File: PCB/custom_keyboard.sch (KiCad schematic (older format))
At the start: 33 parts

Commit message: Keyboard matrix
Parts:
- removed MX?: MX-NoLED, symbol MX_Alps_Hybrid:MX-NoLED
- added D? (x23): SOD-123, symbol Device:D_Small
- added SW? (x23): CherryMX, symbol CherryMX:CherryMX
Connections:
- net labels added: ROT1_COL, ROT1_ROW, ROT2_COL, ROT2_ROW
- wire segments 104 -> 248

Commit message: RGB LED Matrix
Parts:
- removed D? (x6): SOD-123, symbol Device:D_Small
- removed SW? (x6): CherryMX, symbol CherryMX:CherryMX
- added C? (x92): 0.1uF, symbol Device:C_Small
- added D? (x74): SOD-123, symbol Device:D_Small
- added D? (x92): WS2812B, LED_SMD:LED_WS2812B_PLCC4_5.0x5.0mm_P3.2mm, symbol LED:WS2812B
- added R?: 500, symbol Device:R_Small
- added SW?: ESC, symbol CherryMX:CherryMX
- added SW?: `/~, symbol CherryMX:CherryMX
- added SW?: TAB, symbol CherryMX:CherryMX
- added SW?: CAPS, symbol CherryMX:CherryMX
- added SW?: LSHIFT, symbol CherryMX:CherryMX
- added SW?: 1, symbol CherryMX:CherryMX
- added SW?: Q, symbol CherryMX:CherryMX
- added SW?: A, symbol CherryMX:CherryMX
- added SW?: Z, symbol CherryMX:CherryMX
- added SW?: F1, symbol CherryMX:CherryMX
- added SW?: 2, symbol CherryMX:CherryMX
- added SW?: W, symbol CherryMX:CherryMX
- added SW?: S, symbol CherryMX:CherryMX
- added SW?: X, symbol CherryMX:CherryMX
- added SW?: F2, symbol CherryMX:CherryMX
- added SW?: 3, symbol CherryMX:CherryMX
- added SW?: E, symbol CherryMX:CherryMX
- added SW?: D, symbol CherryMX:CherryMX
- added SW?: C, symbol CherryMX:CherryMX
- added SW?: F3, symbol CherryMX:CherryMX
- added SW?: 4, symbol CherryMX:CherryMX
- added SW?: R, symbol CherryMX:CherryMX
- added SW?: F, symbol CherryMX:CherryMX
- added SW?: V, symbol CherryMX:CherryMX
- added SW?: B, symbol CherryMX:CherryMX
- added SW?: G, symbol CherryMX:CherryMX
- added SW?: T, symbol CherryMX:CherryMX
- added SW?: 5, symbol CherryMX:CherryMX
- added SW?: F4, symbol CherryMX:CherryMX
- added SW?: N, symbol CherryMX:CherryMX
- added SW?: M, symbol CherryMX:CherryMX
- added SW?: ,/<, symbol CherryMX:CherryMX
- added SW?: F5, symbol CherryMX:CherryMX
- added SW?: 6, symbol CherryMX:CherryMX
- added SW?: Y, symbol CherryMX:CherryMX
- added SW?: H, symbol CherryMX:CherryMX
- added SW?: J, symbol CherryMX:CherryMX
- added SW?: U, symbol CherryMX:CherryMX
- added SW?: 7, symbol CherryMX:CherryMX
- added SW?: F6, symbol CherryMX:CherryMX
- added SW?: F7, symbol CherryMX:CherryMX
- added SW?: 8, symbol CherryMX:CherryMX
- added SW?: I, symbol CherryMX:CherryMX
- added SW?: K, symbol CherryMX:CherryMX
- added SW?: F8, symbol CherryMX:CherryMX
- added SW?: 9, symbol CherryMX:CherryMX
- added SW?: O, symbol CherryMX:CherryMX
- added SW?: L, symbol CherryMX:CherryMX
- added SW?: ./>, symbol CherryMX:CherryMX
- added SW?: F9, symbol CherryMX:CherryMX
- added SW?: F10, symbol CherryMX:CherryMX
- added SW?: F11, symbol CherryMX:CherryMX
- added SW?: F12, symbol CherryMX:CherryMX
- added SW?: PSCR, symbol CherryMX:CherryMX
- added SW?: 0, symbol CherryMX:CherryMX
- added SW?: -/_, symbol CherryMX:CherryMX
- added SW?: =/+, symbol CherryMX:CherryMX
- added SW?: BACKSPACE, symbol CherryMX:CherryMX
- added SW?: INS, symbol CherryMX:CherryMX
- added SW?: HOME, symbol CherryMX:CherryMX
- added SW?: PGUP, symbol CherryMX:CherryMX
- added SW?: P, symbol CherryMX:CherryMX
- added SW?: [/{, symbol CherryMX:CherryMX
- added SW?: ]/}, symbol CherryMX:CherryMX
- added SW?: \\, symbol CherryMX:CherryMX
- added SW?: DELETE, symbol CherryMX:CherryMX
- added SW?: END, symbol CherryMX:CherryMX
- added SW?: PGDN, symbol CherryMX:CherryMX
- added SW?: ;/:, symbol CherryMX:CherryMX
- added SW?: '/\", symbol CherryMX:CherryMX
- added SW?: ENTER, symbol CherryMX:CherryMX
- added SW?: RSHIFT, symbol CherryMX:CherryMX
- added SW?: /, symbol CherryMX:CherryMX
- added SW?: UP, symbol CherryMX:CherryMX
- SW?: value CherryMX -> M1
- SW?: value CherryMX -> M5
- SW?: value CherryMX -> M2
- SW?: value CherryMX -> M3
- SW?: value CherryMX -> M4
- SW?: value CherryMX -> RIGHT
- SW?: value CherryMX -> LCTRL
- SW?: value CherryMX -> LGUI
- SW?: value CherryMX -> LALT
- SW?: value CherryMX -> SPACE
- SW?: value CherryMX -> RALT
- SW?: value CherryMX -> RGUI
- SW?: value CherryMX -> MENU
- SW?: value CherryMX -> RCTRL
- SW?: value CherryMX -> LEFT
- SW?: value CherryMX -> DOWN
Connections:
- net ROT1_COL is gone; now on net COL17: ROT1.S1
- net ROT2_ROW is gone; now on net ROT1_ROW: D?.1 (K)
- net +5V: now also C?.1, C?.1, C?.1, C?.1, C?.1, C?.1, C?.1, C?.1, C?.1, C?.1, C?.1, C?.1, C?.1, C?.1, C?.1, C?.1, C?.1, C?.1, C?.1, C?.1, C?.1, C?.1, C?.1, C?.1, C?.1, C?.1, C?.1, C?.1, C?.1, C?.1, C?.1, C?.1, C?.1, C?.1, C?.1, C?.1, C?.1, C?.1, C?.1, C?.1, C?.1, C?.1, C?.1, C?.1, C?.1, C?.1, C?.1, C?.1, C?.1, C?.1, C?.1, C?.1, C?.1, C?.1, C?.1, C?.1, C?.1, C?.1, C?.1, C?.1, C?.1, C?.1, C?.1, C?.1, C?.1, C?.1, C?.1, C?.1, C?.1, C?.1, C?.1, C?.1, C?.1, C?.1, C?.1, C?.1, C?.1, C?.1, C?.1, C?.1, C?.1, C?.1, C?.1, C?.1, C?.1, C?.1, C?.1, C?.1, C?.1, C?.1, C?.1, C?.1, D?.1 (VDD), D?.1 (VDD), D?.1 (VDD), D?.1 (VDD), D?.1 (VDD), D?.1 (VDD), D?.1 (VDD), D?.1 (VDD), D?.1 (VDD), D?.1 (VDD), D?.1 (VDD), D?.1 (VDD), D?.1 (VDD), D?.1 (VDD), D?.1 (VDD), D?.1 (VDD), D?.1 (VDD), D?.1 (VDD), D?.1 (VDD), D?.1 (VDD), D?.1 (VDD), D?.1 (VDD), D?.1 (VDD), D?.1 (VDD), D?.1 (VDD), D?.1 (VDD), D?.1 (VDD), D?.1 (VDD), D?.1 (VDD), D?.1 (VDD), D?.1 (VDD), D?.1 (VDD), D?.1 (VDD), D?.1 (VDD), D?.1 (VDD), D?.1 (VDD), D?.1 (VDD), D?.1 (VDD), D?.1 (VDD), D?.1 (VDD), D?.1 (VDD), D?.1 (VDD), D?.1 (VDD), D?.1 (VDD), D?.1 (VDD), D?.1 (VDD), D?.1 (VDD), D?.1 (VDD), D?.1 (VDD), D?.1 (VDD), D?.1 (VDD), D?.1 (VDD), D?.1 (VDD), D?.1 (VDD), D?.1 (VDD), D?.1 (VDD), D?.1 (VDD), D?.1 (VDD), D?.1 (VDD), D?.1 (VDD), D?.1 (VDD), D?.1 (VDD), D?.1 (VDD), D?.1 (VDD), D?.1 (VDD), D?.1 (VDD), D?.1 (VDD), D?.1 (VDD), D?.1 (VDD), D?.1 (VDD), D?.1 (VDD), D?.1 (VDD), D?.1 (VDD), D?.1 (VDD), D?.1 (VDD), D?.1 (VDD), D?.1 (VDD), D?.1 (VDD), D?.1 (VDD), D?.1 (VDD), D?.1 (VDD), D?.1 (VDD), D?.1 (VDD), D?.1 (VDD), D?.1 (VDD), D?.1 (VDD), D?.1 (VDD), D?.1 (VDD), D?.1 (VDD), D?.1 (VDD), D?.1 (VDD), D?.1 (VDD)
- net BKL_DATA_IN: now also R?.1
- net COL1: now also SW?.1, SW?.1, SW?.1, SW?.1, SW?.1
- net COL10: now also SW?.1, SW?.1, SW?.1, SW?.1, SW?.1
- net COL11: now also SW?.1, SW?.1, SW?.1, SW?.1, SW?.1
- net COL12: now also SW?.1, SW?.1, SW?.1, SW?.1
- net COL13: now also SW?.1, SW?.1, SW?.1
- net COL14: now also SW?.1, SW?.1, SW?.1, SW?.1, SW?.1
- net COL15: now also SW?.1, SW?.1, SW?.1
- net COL16: now also SW?.1, SW?.1, SW?.1
- net COL17: now also SW?.1, SW?.1
- net COL2: now also SW?.1, SW?.1, SW?.1, SW?.1
- net COL3: now also SW?.1, SW?.1, SW?.1, SW?.1, SW?.1
- net COL4: now also SW?.1, SW?.1, SW?.1, SW?.1, SW?.1
- net COL5: now also SW?.1, SW?.1, SW?.1, SW?.1, SW?.1
- net COL6: now also SW?.1, SW?.1, SW?.1, SW?.1, SW?.1
- net COL7: now also SW?.1, SW?.1, SW?.1, SW?.1, SW?.1
- net COL8: now also SW?.1, SW?.1, SW?.1, SW?.1, SW?.1
- net COL9: now also SW?.1, SW?.1, SW?.1, SW?.1, SW?.1
- net GND: now also C?.2, C?.2, C?.2, C?.2, C?.2, C?.2, C?.2, C?.2, C?.2, C?.2, C?.2, C?.2, C?.2, C?.2, C?.2, C?.2, C?.2, C?.2, C?.2, C?.2, C?.2, C?.2, C?.2, C?.2, C?.2, C?.2, C?.2, C?.2, C?.2, C?.2, C?.2, C?.2, C?.2, C?.2, C?.2, C?.2, C?.2, C?.2, C?.2, C?.2, C?.2, C?.2, C?.2, C?.2, C?.2, C?.2, C?.2, C?.2, C?.2, C?.2, C?.2, C?.2, C?.2, C?.2, C?.2, C?.2, C?.2, C?.2, C?.2, C?.2, C?.2, C?.2, C?.2, C?.2, C?.2, C?.2, C?.2, C?.2, C?.2, C?.2, C?.2, C?.2, C?.2, C?.2, C?.2, C?.2, C?.2, C?.2, C?.2, C?.2, C?.2, C?.2, C?.2, C?.2, C?.2, C?.2, C?.2, C?.2, C?.2, C?.2, C?.2, C?.2, D?.3 (VSS), D?.3 (VSS), D?.3 (VSS), D?.3 (VSS), D?.3 (VSS), D?.3 (VSS), D?.3 (VSS), D?.3 (VSS), D?.3 (VSS), D?.3 (VSS), D?.3 (VSS), D?.3 (VSS), D?.3 (VSS), D?.3 (VSS), D?.3 (VSS), D?.3 (VSS), D?.3 (VSS), D?.3 (VSS), D?.3 (VSS), D?.3 (VSS), D?.3 (VSS), D?.3 (VSS), D?.3 (VSS), D?.3 (VSS), D?.3 (VSS), D?.3 (VSS), D?.3 (VSS), D?.3 (VSS), D?.3 (VSS), D?.3 (VSS), D?.3 (VSS), D?.3 (VSS), D?.3 (VSS), D?.3 (VSS), D?.3 (VSS), D?.3 (VSS), D?.3 (VSS), D?.3 (VSS), D?.3 (VSS), D?.3 (VSS), D?.3 (VSS), D?.3 (VSS), D?.3 (VSS), D?.3 (VSS), D?.3 (VSS), D?.3 (VSS), D?.3 (VSS), D?.3 (VSS), D?.3 (VSS), D?.3 (VSS), D?.3 (VSS), D?.3 (VSS), D?.3 (VSS), D?.3 (VSS), D?.3 (VSS), D?.3 (VSS), D?.3 (VSS), D?.3 (VSS), D?.3 (VSS), D?.3 (VSS), D?.3 (VSS), D?.3 (VSS), D?.3 (VSS), D?.3 (VSS), D?.3 (VSS), D?.3 (VSS), D?.3 (VSS), D?.3 (VSS), D?.3 (VSS), D?.3 (VSS), D?.3 (VSS), D?.3 (VSS), D?.3 (VSS), D?.3 (VSS), D?.3 (VSS), D?.3 (VSS), D?.3 (VSS), D?.3 (VSS), D?.3 (VSS), D?.3 (VSS), D?.3 (VSS), D?.3 (VSS), D?.3 (VSS), D?.3 (VSS), D?.3 (VSS), D?.3 (VSS), D?.3 (VSS), D?.3 (VSS), D?.3 (VSS), D?.3 (VSS), D?.3 (VSS), D?.3 (VSS)
- net ROT1_ROW: now also D?.1 (K), D?.1 (K), D?.1 (K), D?.1 (K), D?.1 (K), D?.1 (K), D?.1 (K), D?.1 (K), D?.1 (K), D?.1 (K), D?.1 (K), D?.1 (K), D?.1 (K), D?.1 (K)
- net ROW1: now also D?.1 (K), D?.1 (K), D?.1 (K), D?.1 (K), D?.1 (K), D?.1 (K), D?.1 (K), D?.1 (K), D?.1 (K), D?.1 (K), D?.1 (K), D?.1 (K), D?.1 (K), D?.1 (K), D?.1 (K), D?.1 (K), D?.1 (K), D?.1 (K)
- net ROW2: now also D?.1 (K), D?.1 (K), D?.1 (K), D?.1 (K), D?.1 (K), D?.1 (K), D?.1 (K), D?.1 (K), D?.1 (K), D?.1 (K), D?.1 (K), D?.1 (K), D?.1 (K), D?.1 (K), D?.1 (K), D?.1 (K), D?.1 (K)
- net ROW3: now also D?.1 (K), D?.1 (K), D?.1 (K), D?.1 (K), D?.1 (K), D?.1 (K), D?.1 (K), D?.1 (K), D?.1 (K), D?.1 (K), D?.1 (K), D?.1 (K), D?.1 (K)
- net ROW4: now also D?.1 (K), D?.1 (K), D?.1 (K), D?.1 (K), D?.1 (K), D?.1 (K), D?.1 (K), D?.1 (K), D?.1 (K), D?.1 (K), D?.1 (K), D?.1 (K), D?.1 (K)
- new net: D?.2 (A), SW?.2 (x74)
- new net: D?.2 (DOUT), D?.4 (DIN) (x82)
- new net: D?.4 (DIN), R?.2
- new net DOUT1: D?.2 (DOUT), D?.4 (DIN)
- new net DOUT2: D?.2 (DOUT), D?.4 (DIN)
- new net DOUT3: D?.2 (DOUT), D?.4 (DIN)
- new net DOUT4: D?.2 (DOUT), D?.4 (DIN)
- new net DOUT5: D?.2 (DOUT), D?.4 (DIN)
- new net DOUT6: D?.2 (DOUT), D?.4 (DIN)
- new net DOUT7: D?.2 (DOUT), D?.4 (DIN)
- new net DOUT8: D?.2 (DOUT), D?.4 (DIN)
- new net DOUT9: D?.2 (DOUT), D?.4 (DIN)
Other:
- note added: "0"
- note added: "1"
- note added: "10"
- note added: "10\n"
- note added: "11"
- note added: "12"
- note added: "13"
- note added: "14"
- note added: "15"
- note added: "16"
- note added: "17"
- note added: "2"
- note added: "3"
- note added: "4"
- note added: "5"
- note added: "6"
- note added: "7"
- note added: "7\n"
- note added: "8"
- note added: "9"
- moved on the sheet: C?, D?, J?, R?, ROT1, ROT2, SW?, U?, Y?

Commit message: Added outlines
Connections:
- net BKL_DATA_IN: now also U?.51 (PA0)
- net COL0: now also U?.47 (PA4)
- net COL1: now also U?.46 (PA5)
- net COL10: now also U?.36 (PC1)
- net COL11: now also U?.35 (PC0)
- net COL14: now also U?.32 (PD7)
- net COL15: now also U?.31 (PD6)
- net COL16: now also U?.30 (PD5)
- net COL17: now also U?.29 (PD4)
- net COL2: now also U?.45 (PA6)
- net COL3: now also U?.44 (PA7)
- net COL4: now also U?.42 (PC7)
- net COL5: now also U?.41 (PC6)
- net COL6: now also U?.40 (PC5)
- net COL7: now also U?.39 (PC4)
- net COL8: now also U?.38 (PC3)
- net COL9: now also U?.37 (PC2)
- net ENCODER_A: now also U?.50 (PA1)
- net ENCODER_B1: now also U?.49 (PA2)
- net ENCODER_B2: now also U?.48 (PA3)
- net KEYBOARD_SCL: now also U?.25 (PD0)
- net KEYBOARD_SDA: now also U?.26 (PD1)
- net KEYBOARD_SIGNAL: now also U?.14 (PB4)
- net MISO: now also U?.13 (PB3)
- net MOSI: now also U?.12 (PB2)
- net ROT1_ROW: now also U?.56 (PF5)
- net ROW1: now also U?.57 (PF4)
- net ROW2: now also U?.58 (PF3)
- net ROW3: now also U?.59 (PF2)
- net ROW4: now also U?.60 (PF1)
- net ROW5: now also U?.61 (PF0)
- net SCLK: now also U?.11 (PB1)
- net SS: now also U?.10 (PB0)
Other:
- moved on the sheet: C?, D?, J?, R?, ROT1, ROT2, SW?, U?, Y?

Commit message: Corrected most electrical rules checks
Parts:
- removed C? (x91): 0.1uF, symbol Device:C_Small
- removed D? (x91): WS2812B, LED_SMD:LED_WS2812B_PLCC4_5.0x5.0mm_P3.2mm, symbol LED:WS2812B
- added C1, C10, C11, C12, C13, C14, C15, C16, C17, C18, C19, C2, C21, C22, C23, C24, C25, C26, C27, C28, C29, C3, C30, C31, C32, C33, C34, C35, C36, C37, C38, C39, C4, C40, C41, C42, C43, C44, C45, C46, C47, C48, C49, C5, C50, C51, C52, C53, C54, C55, C56, C57, C58, C59, C6, C60, C61, C62, C63, C64, C65, C66, C67, C68, C69, C7, C70, C71, C72, C73, C74, C75, C76, C77, C78, C79, C8, C80, C81, C82, C83, C84, C85, C86, C87, C88, C89, C9, C90, C91, C92: 0.1uF, symbol Device:C_Small
- added D1, D10, D100, D101, D102, D103, D109, D110, D111, D112, D113, D114, D115, D116, D117, D123, D124, D125, D126, D127, D128, D129, D130, D131, D137, D138, D139, D140, D141, D142, D143, D144, D145, D16, D17, D18, D19, D2, D20, D21, D22, D23, D24, D3, D37, D38, D39, D4, D40, D41, D42, D43, D44, D45, D5, D52, D53, D54, D55, D56, D57, D58, D59, D6, D60, D66, D67, D68, D69, D7, D70, D71, D72, D73, D74, D8, D80, D81, D82, D83, D84, D85, D86, D87, D88, D9, D95, D96, D97, D98, D99: WS2812B, LED_SMD:LED_WS2812B_PLCC4_5.0x5.0mm_P3.2mm, symbol LED:WS2812B
- added OL1: OLED, symbol kbd:OLED
- gave numbers to parts that had none: 215
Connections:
- net +5V: now also C1.1, C10.1, C11.1, C12.1, C13.1, C14.1, C15.1, C16.1, C17.1, C18.1, C19.1, C2.1, C21.1, C22.1, C23.1, C24.1, C25.1, C26.1, C27.1, C28.1, C29.1, C3.1, C30.1, C31.1, C32.1, C33.1, C34.1, C35.1, C36.1, C37.1, C38.1, C39.1, C4.1, C40.1, C41.1, C42.1, C43.1, C44.1, C45.1, C46.1, C47.1, C48.1, C49.1, C5.1, C50.1, C51.1, C52.1, C53.1, C54.1, C55.1, C56.1, C57.1, C58.1, C59.1, C6.1, C60.1, C61.1, C62.1, C63.1, C64.1, C65.1, C66.1, C67.1, C68.1, C69.1, C7.1, C70.1, C71.1, C72.1, C73.1, C74.1, C75.1, C76.1, C77.1, C78.1, C79.1, C8.1, C80.1, C81.1, C82.1, C83.1, C84.1, C85.1, C86.1, C87.1, C88.1, C89.1, C9.1, C90.1, C91.1, C92.1, D1.1 (VDD), D10.1 (VDD), D100.1 (VDD), D101.1 (VDD), D102.1 (VDD), D103.1 (VDD), D109.1 (VDD), D110.1 (VDD), D111.1 (VDD), D112.1 (VDD), D113.1 (VDD), D114.1 (VDD), D115.1 (VDD), D116.1 (VDD), D117.1 (VDD), D123.1 (VDD), D124.1 (VDD), D125.1 (VDD), D126.1 (VDD), D127.1 (VDD), D128.1 (VDD), D129.1 (VDD), D130.1 (VDD), D131.1 (VDD), D137.1 (VDD), D138.1 (VDD), D139.1 (VDD), D140.1 (VDD), D141.1 (VDD), D142.1 (VDD), D143.1 (VDD), D144.1 (VDD), D145.1 (VDD), D16.1 (VDD), D17.1 (VDD), D18.1 (VDD), D19.1 (VDD), D2.1 (VDD), D20.1 (VDD), D21.1 (VDD), D22.1 (VDD), D23.1 (VDD), D24.1 (VDD), D3.1 (VDD), D37.1 (VDD), D38.1 (VDD), D39.1 (VDD), D4.1 (VDD), D40.1 (VDD), D41.1 (VDD), D42.1 (VDD), D43.1 (VDD), D44.1 (VDD), D45.1 (VDD), D5.1 (VDD), D52.1 (VDD), D53.1 (VDD), D54.1 (VDD), D55.1 (VDD), D56.1 (VDD), D57.1 (VDD), D58.1 (VDD), D59.1 (VDD), D6.1 (VDD), D60.1 (VDD), D66.1 (VDD), D67.1 (VDD), D68.1 (VDD), D69.1 (VDD), D7.1 (VDD), D70.1 (VDD), D71.1 (VDD), D72.1 (VDD), D73.1 (VDD), D74.1 (VDD), D8.1 (VDD), D80.1 (VDD), D81.1 (VDD), D82.1 (VDD), D83.1 (VDD), D84.1 (VDD), D85.1 (VDD), D86.1 (VDD), D87.1 (VDD), D88.1 (VDD), D9.1 (VDD), D95.1 (VDD), D96.1 (VDD), D97.1 (VDD), D98.1 (VDD), D99.1 (VDD), OL1.3 (VCC)
- net DOUT1: now also D137.4 (DIN), D6.2 (DOUT)
- net DOUT2: now also D138.4 (DIN), D7.2 (DOUT)
- net DOUT3: now also D139.4 (DIN), D8.2 (DOUT)
- net DOUT4: now also D140.4 (DIN), D9.2 (DOUT)
- net DOUT5: now also D10.2 (DOUT), D141.4 (DIN)
- net DOUT6: now also D142.4 (DIN), D16.2 (DOUT)
- net DOUT7: now also D143.4 (DIN), D17.2 (DOUT)
- net DOUT8: now also D144.4 (DIN), D2.2 (DOUT)
- net DOUT9: now also D1.2 (DOUT), D145.4 (DIN)
- net GND: now also C1.2, C10.2, C11.2, C12.2, C13.2, C14.2, C15.2, C16.2, C17.2, C18.2, C19.2, C2.2, C21.2, C22.2, C23.2, C24.2, C25.2, C26.2, C27.2, C28.2, C29.2, C3.2, C30.2, C31.2, C32.2, C33.2, C34.2, C35.2, C36.2, C37.2, C38.2, C39.2, C4.2, C40.2, C41.2, C42.2, C43.2, C44.2, C45.2, C46.2, C47.2, C48.2, C49.2, C5.2, C50.2, C51.2, C52.2, C53.2, C54.2, C55.2, C56.2, C57.2, C58.2, C59.2, C6.2, C60.2, C61.2, C62.2, C63.2, C64.2, C65.2, C66.2, C67.2, C68.2, C69.2, C7.2, C70.2, C71.2, C72.2, C73.2, C74.2, C75.2, C76.2, C77.2, C78.2, C79.2, C8.2, C80.2, C81.2, C82.2, C83.2, C84.2, C85.2, C86.2, C87.2, C88.2, C89.2, C9.2, C90.2, C91.2, C92.2, D1.3 (VSS), D10.3 (VSS), D100.3 (VSS), D101.3 (VSS), D102.3 (VSS), D103.3 (VSS), D109.3 (VSS), D110.3 (VSS), D111.3 (VSS), D112.3 (VSS), D113.3 (VSS), D114.3 (VSS), D115.3 (VSS), D116.3 (VSS), D117.3 (VSS), D123.3 (VSS), D124.3 (VSS), D125.3 (VSS), D126.3 (VSS), D127.3 (VSS), D128.3 (VSS), D129.3 (VSS), D130.3 (VSS), D131.3 (VSS), D137.3 (VSS), D138.3 (VSS), D139.3 (VSS), D140.3 (VSS), D141.3 (VSS), D142.3 (VSS), D143.3 (VSS), D144.3 (VSS), D145.3 (VSS), D16.3 (VSS), D17.3 (VSS), D18.3 (VSS), D19.3 (VSS), D2.3 (VSS), D20.3 (VSS), D21.3 (VSS), D22.3 (VSS), D23.3 (VSS), D24.3 (VSS), D3.3 (VSS), D37.3 (VSS), D38.3 (VSS), D39.3 (VSS), D4.3 (VSS), D40.3 (VSS), D41.3 (VSS), D42.3 (VSS), D43.3 (VSS), D44.3 (VSS), D45.3 (VSS), D5.3 (VSS), D52.3 (VSS), D53.3 (VSS), D54.3 (VSS), D55.3 (VSS), D56.3 (VSS), D57.3 (VSS), D58.3 (VSS), D59.3 (VSS), D6.3 (VSS), D60.3 (VSS), D66.3 (VSS), D67.3 (VSS), D68.3 (VSS), D69.3 (VSS), D7.3 (VSS), D70.3 (VSS), D71.3 (VSS), D72.3 (VSS), D73.3 (VSS), D74.3 (VSS), D8.3 (VSS), D80.3 (VSS), D81.3 (VSS), D82.3 (VSS), D83.3 (VSS), D84.3 (VSS), D85.3 (VSS), D86.3 (VSS), D87.3 (VSS), D88.3 (VSS), D9.3 (VSS), D95.3 (VSS), D96.3 (VSS), D97.3 (VSS), D98.3 (VSS), D99.3 (VSS), OL1.4 (GND)
- net KEYBOARD_SCL: now also OL1.2 (SCL)
- net KEYBOARD_SDA: now also OL1.1 (SDA)
- net at D25.2 (DOUT): now also D1.4 (DIN)
- new net: D2.4 (DIN), D3.2 (DOUT)
- new net: D3.4 (DIN), D4.2 (DOUT)
- new net: D4.4 (DIN), D60.2 (DOUT)
- new net: D60.4 (DIN), D74.2 (DOUT)
- new net: D74.4 (DIN), D88.2 (DOUT)
- new net: D103.2 (DOUT), D88.4 (DIN)
- new net: D103.4 (DIN), D117.2 (DOUT)
- new net: D117.4 (DIN), D131.2 (DOUT)
- new net: D131.4 (DIN), D145.2 (DOUT)
- new net: D17.4 (DIN), D37.2 (DOUT)
- new net: D37.4 (DIN), D45.2 (DOUT)
- new net: D45.4 (DIN), D59.2 (DOUT)
- new net: D59.4 (DIN), D73.2 (DOUT)
- new net: D73.4 (DIN), D87.2 (DOUT)
- new net: D102.2 (DOUT), D87.4 (DIN)
- new net: D102.4 (DIN), D116.2 (DOUT)
- new net: D116.4 (DIN), D130.2 (DOUT)
- new net: D130.4 (DIN), D144.2 (DOUT)
- new net: D16.4 (DIN), D24.2 (DOUT)
- new net: D24.4 (DIN), D44.2 (DOUT)
- new net: D44.4 (DIN), D58.2 (DOUT)
- new net: D58.4 (DIN), D72.2 (DOUT)
- new net: D72.4 (DIN), D86.2 (DOUT)
- new net: D101.2 (DOUT), D86.4 (DIN)
- new net: D101.4 (DIN), D115.2 (DOUT)
- new net: D115.4 (DIN), D129.2 (DOUT)
- new net: D129.4 (DIN), D143.2 (DOUT)
- new net: D10.4 (DIN), D23.2 (DOUT)
- new net: D23.4 (DIN), D43.2 (DOUT)
- new net: D43.4 (DIN), D57.2 (DOUT)
- new net: D57.4 (DIN), D71.2 (DOUT)
- new net: D71.4 (DIN), D85.2 (DOUT)
- new net: D100.2 (DOUT), D85.4 (DIN)
- new net: D100.4 (DIN), D114.2 (DOUT)
- new net: D114.4 (DIN), D128.2 (DOUT)
- new net: D128.4 (DIN), D142.2 (DOUT)
- new net: D22.2 (DOUT), D9.4 (DIN)
- new net: D22.4 (DIN), D42.2 (DOUT)
- new net: D42.4 (DIN), D56.2 (DOUT)
- new net: D56.4 (DIN), D70.2 (DOUT)
- new net: D70.4 (DIN), D84.2 (DOUT)
- new net: D84.4 (DIN), D99.2 (DOUT)
- new net: D113.2 (DOUT), D99.4 (DIN)
- new net: D113.4 (DIN), D127.2 (DOUT)
- new net: D127.4 (DIN), D141.2 (DOUT)
- new net: D21.2 (DOUT), D8.4 (DIN)
- new net: D21.4 (DIN), D41.2 (DOUT)
- new net: D41.4 (DIN), D55.2 (DOUT)
- new net: D55.4 (DIN), D69.2 (DOUT)
- new net: D69.4 (DIN), D83.2 (DOUT)
- new net: D83.4 (DIN), D98.2 (DOUT)
- new net: D112.2 (DOUT), D98.4 (DIN)
- new net: D112.4 (DIN), D126.2 (DOUT)
- new net: D126.4 (DIN), D140.2 (DOUT)
- new net: D20.2 (DOUT), D7.4 (DIN)
- new net: D20.4 (DIN), D40.2 (DOUT)
- new net: D40.4 (DIN), D54.2 (DOUT)
- new net: D54.4 (DIN), D68.2 (DOUT)
- new net: D68.4 (DIN), D82.2 (DOUT)
- new net: D82.4 (DIN), D97.2 (DOUT)
- new net: D111.2 (DOUT), D97.4 (DIN)
- new net: D111.4 (DIN), D125.2 (DOUT)
- new net: D125.4 (DIN), D139.2 (DOUT)
- new net: D19.2 (DOUT), D6.4 (DIN)
- new net: D19.4 (DIN), D39.2 (DOUT)
- new net: D39.4 (DIN), D53.2 (DOUT)
- new net: D53.4 (DIN), D67.2 (DOUT)
- new net: D67.4 (DIN), D81.2 (DOUT)
- new net: D81.4 (DIN), D96.2 (DOUT)
- new net: D110.2 (DOUT), D96.4 (DIN)
- new net: D110.4 (DIN), D124.2 (DOUT)
- new net: D124.4 (DIN), D138.2 (DOUT)
- new net: D18.2 (DOUT), D5.4 (DIN)
- new net: D18.4 (DIN), D38.2 (DOUT)
- new net: D38.4 (DIN), D52.2 (DOUT)
- new net: D52.4 (DIN), D66.2 (DOUT)
- new net: D66.4 (DIN), D80.2 (DOUT)
- new net: D80.4 (DIN), D95.2 (DOUT)
- new net: D109.2 (DOUT), D95.4 (DIN)
- new net: D109.4 (DIN), D123.2 (DOUT)
- new net: D123.4 (DIN), D137.2 (DOUT)
- no-connect marks 0 -> 16
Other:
- moved on the sheet: C101, C102, C20, D186, D25, J1, R1, R10, Y1

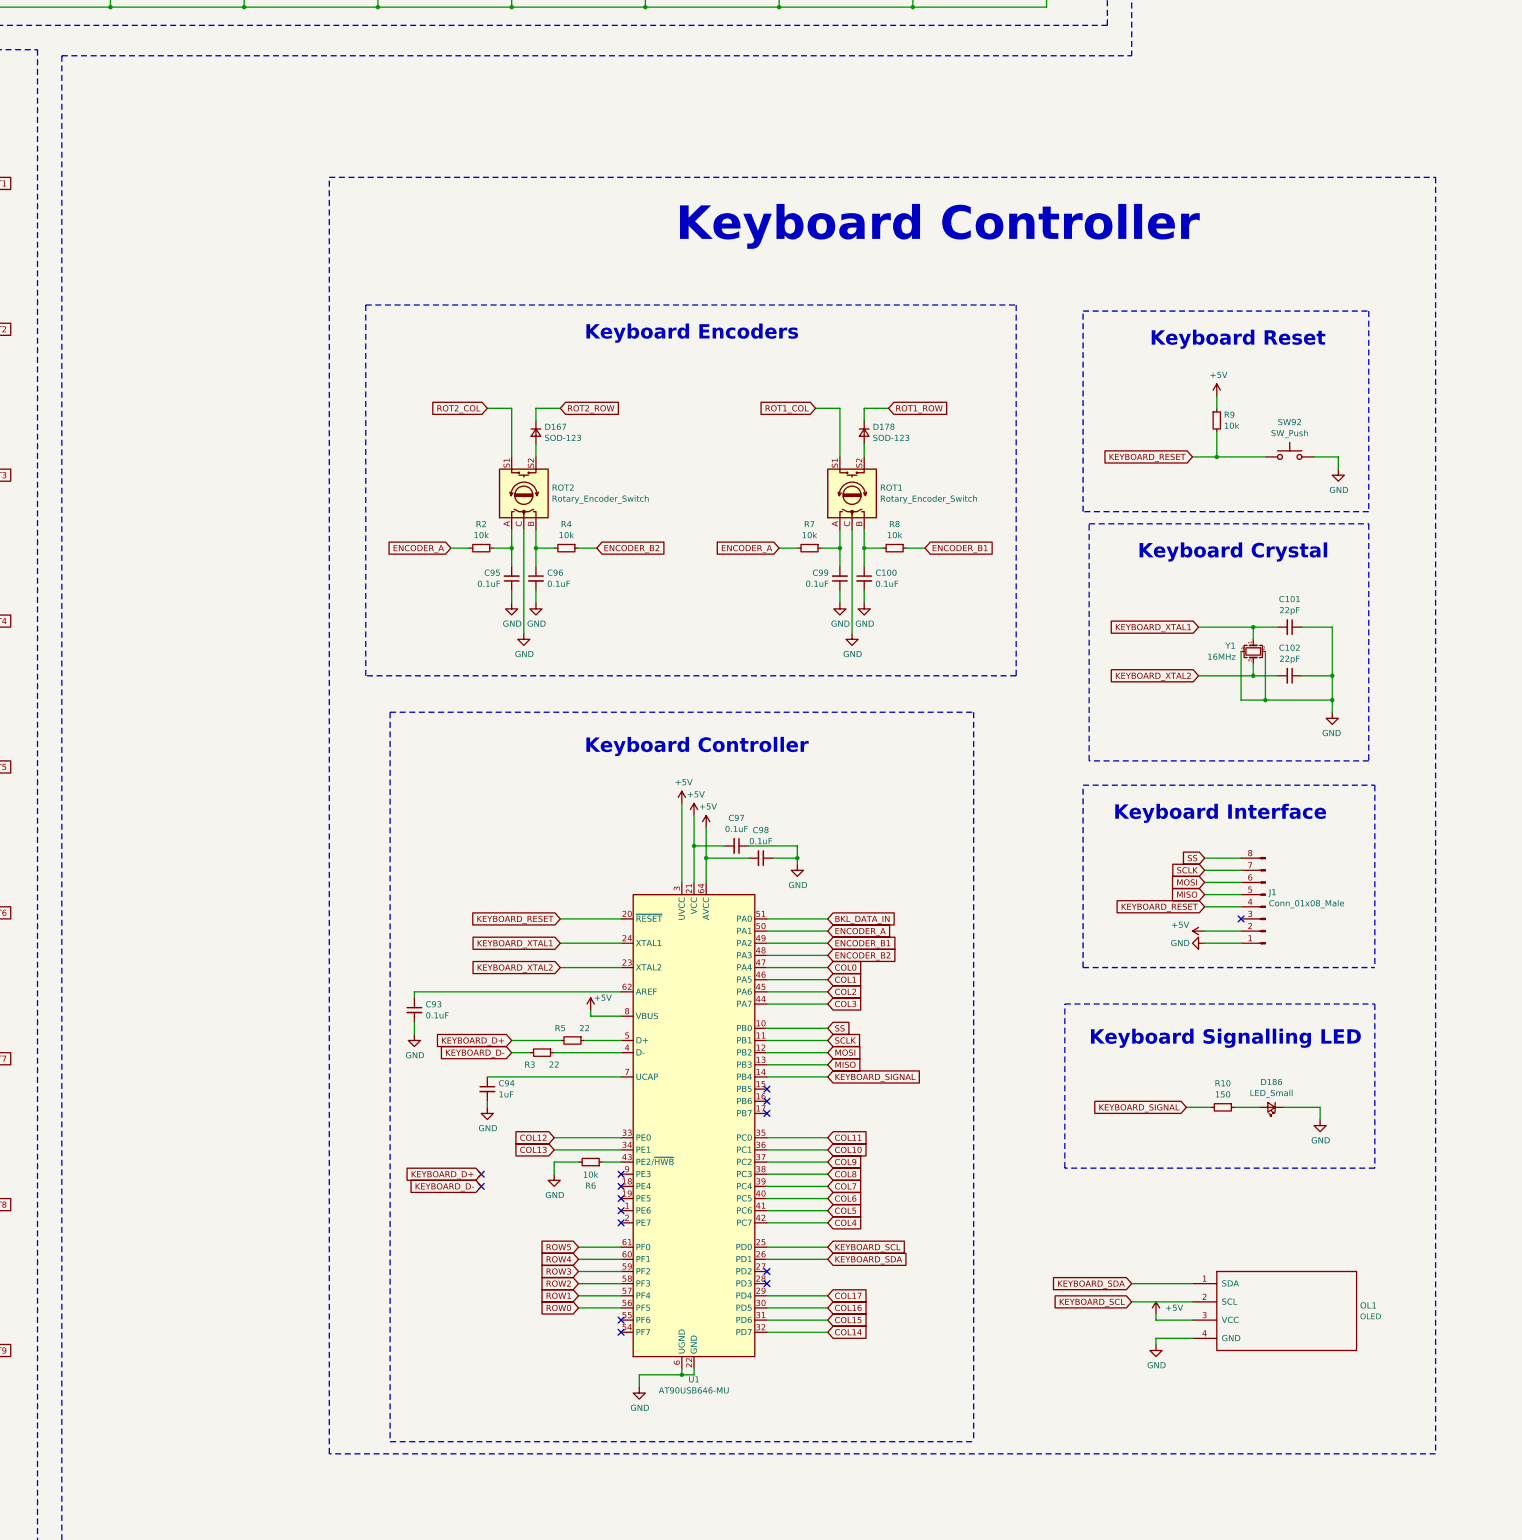
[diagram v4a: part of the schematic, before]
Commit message: Keyboard OLED label
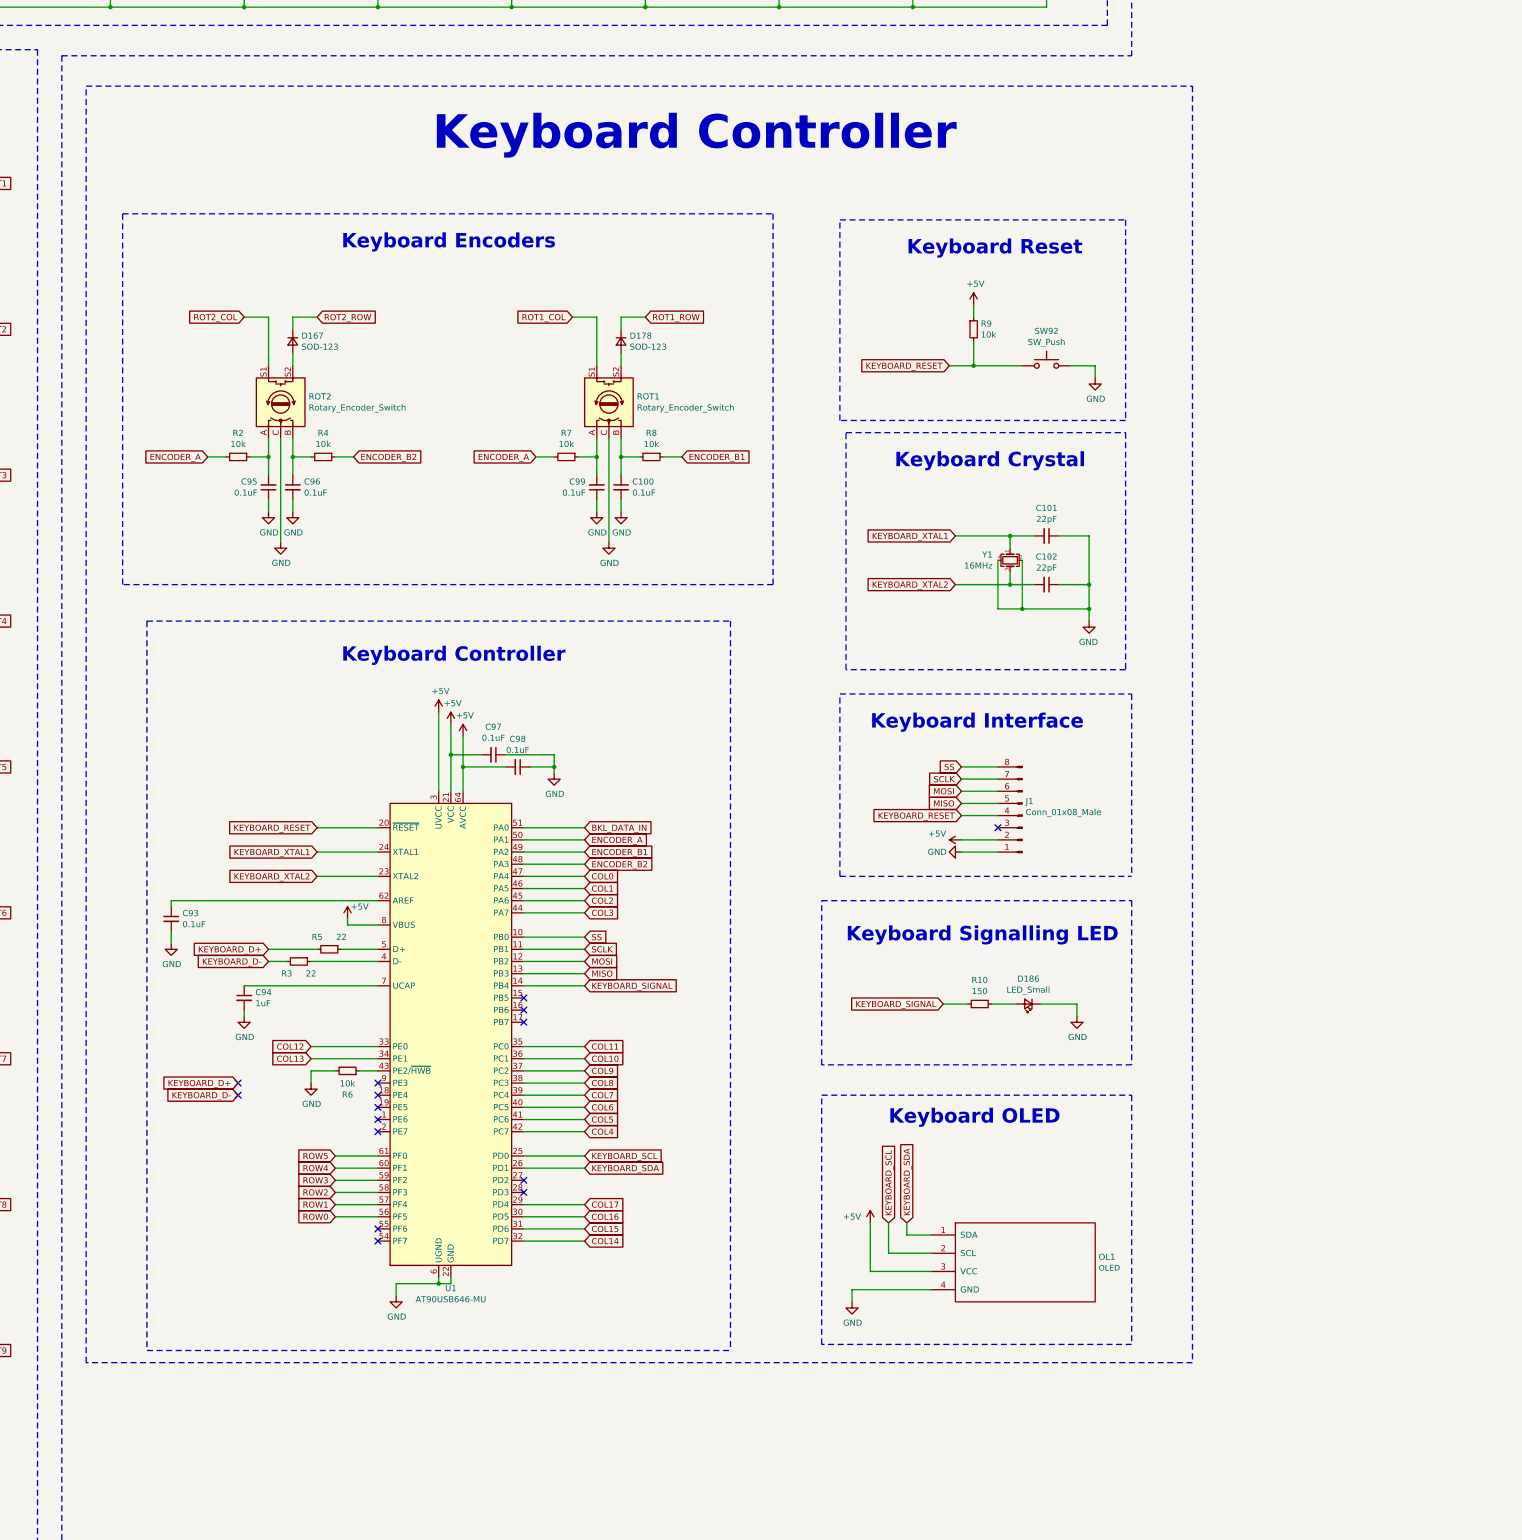
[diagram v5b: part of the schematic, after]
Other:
- note added: "Keyboard OLED"
- moved on the sheet: C100, C101, C102, C93, C94, C95, C96, C97, C98, C99, D167, D178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

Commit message: Imported FE2.1
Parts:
- added IC?: FE2.1, symbol MyConnectors:FE2.1
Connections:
- net KEYBOARD_SCL: now also OL1.1 (SDA); no longer OL1.2 (SCL)
- net KEYBOARD_SDA: now also OL1.2 (SCL); no longer OL1.1 (SDA)
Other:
- moved on the sheet: C1, C10, C100, C101, C102, C11, C12, C13, C14, C15, C16, C17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
